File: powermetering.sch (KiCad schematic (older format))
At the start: 143 parts, among them J1 Conn_01x04, J2 Conn_01x02, J3 Conn_01x02, J4 Conn_01x02, J5 Conn_01x02, T1 Transformer_1P_1S, T2 Transformer_1P_1S, T3 Transformer_1P_1S, U2 ADE9000, U7 LTC4055, Y1 Crystal

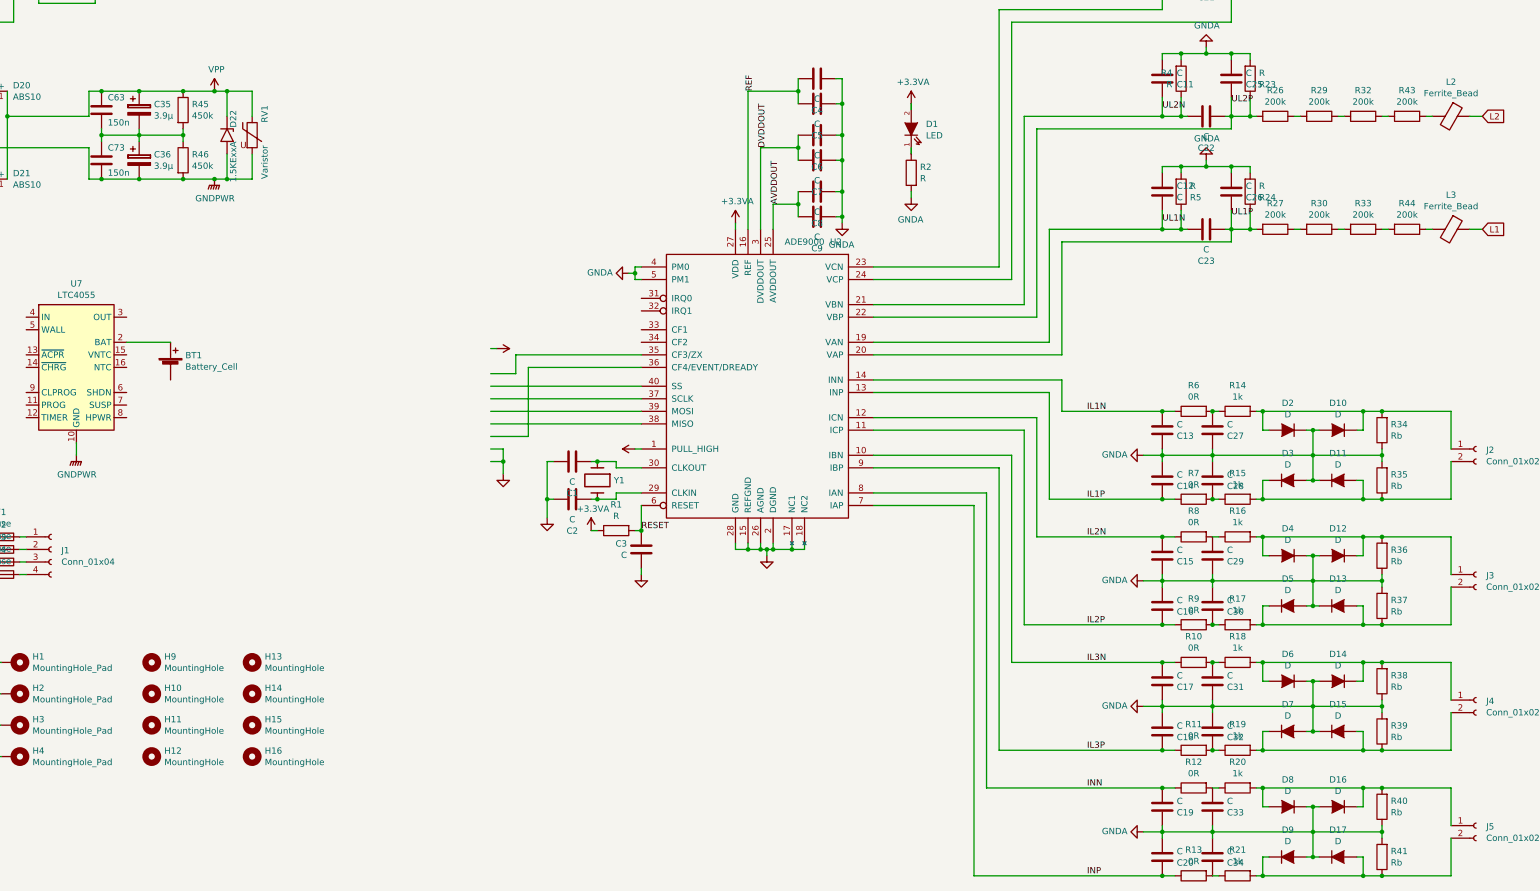
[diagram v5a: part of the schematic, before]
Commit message: Change to bigger housing
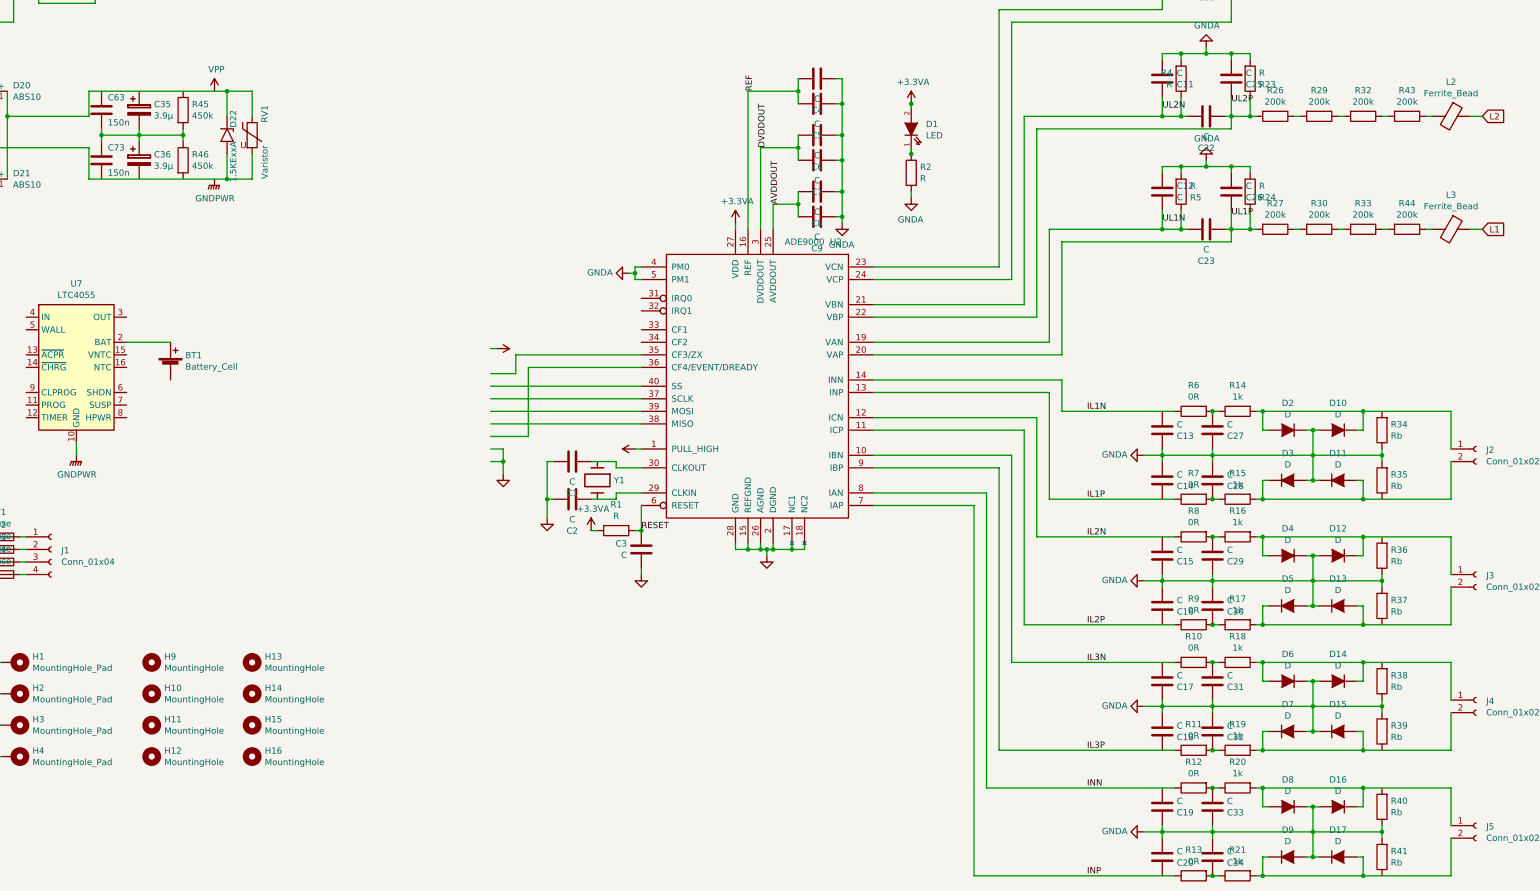
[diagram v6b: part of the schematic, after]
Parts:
- F1, F2, F3, F4: footprint Fuse:Fuse_2920_7451Metric -> Fuse:Fuseholder_Cylinder-6.3x32mm_Schurter_0031-8002_Horizontal_Open
- J1: footprint TerminalBlock_WAGO:TerminalBlock_WAGO-236_2Stift_RM5mm_4pol -> TerminalBlock_Phoenix:TerminalBlock_Phoenix_PT-1,5-4-5.0-H_1x04_P5.00mm_Horizontal
- J2, J3, J4, J5: footprint TerminalBlock_WAGO:TerminalBlock_WAGO-236_2Stift_RM5mm_2pol -> TerminalBlock_Phoenix:TerminalBlock_Phoenix_PT-1,5-2-5.0-H_1x02_P5.00mm_Horizontal
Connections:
- wire segments 444 -> 418
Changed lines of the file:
@@
-EESchema Schematic File Version 4
+EESchema Schematic File Version 5
+LIBS:powermetering-cache
 EELAYER 29 0
 EELAYER END
@@
 F 0 "J1" H 3780 6942 50  0000 L CNN
 F 1 "Conn_01x04" H 3780 6851 50  0000 L CNN
-F 2 "TerminalBlock_WAGO:TerminalBlock_WAGO-236_2Stift_RM5mm_4pol" H 3700 6950 50  0001 C CNN
+F 2 "TerminalBlock_Phoenix:TerminalBlock_Phoenix_PT-1,5-4-5.0-H_1x04_P5.00mm_Horizontal" H 3700 6950 50  0001 C CNN
 F 3 "~" H 3700 6950 50  0001 C CNN
 	1    3700 6950
@@
 F 0 "F1" V 3103 6850 50  0000 C CNN
 F 1 "Fuse" V 3194 6850 50  0000 C CNN
-F 2 "Fuse:Fuse_2920_7451Metric" V 3230 6850 50  0001 C CNN
+F 2 "Fuse:Fuseholder_Cylinder-6.3x32mm_Schurter_0031-8002_Horizontal_Open" V 3230 6850 50  0001 C CNN
 F 3 "" H 3300 6850 50  0001 C CNN
 	1    3300 6850
@@
 F 0 "J2" H 15130 6142 50  0000 L CNN
 F 1 "Conn_01x02" H 15130 6051 50  0000 L CNN
-F 2 "TerminalBlock_WAGO:TerminalBlock_WAGO-236_2Stift_RM5mm_2pol" H 15050 6150 50  0001 C CNN
+F 2 "TerminalBlock_Phoenix:TerminalBlock_Phoenix_PT-1,5-2-5.0-H_1x02_P5.00mm_Horizontal" H 15050 6150 50  0001 C CNN
 F 3 "~" H 15050 6150 50  0001 C CNN
 	1    15050 6150
@@
 $EndComp
 Wire Wire Line
-	14300 6550 14850 6550
-Wire Wire Line
 	14850 6550 14850 6250
-Wire Wire Line
-	14300 5850 14850 5850
 Wire Wire Line
 	14850 5850 14850 6150
@@
 Wire Wire Line
 	13300 6550 13350 6550
-Connection ~ 14300 6550
 Wire Wire Line
 	13300 5850 13350 5850
-Connection ~ 14300 5850
 Wire Wire Line
 	13400 6400 13350 6400
@@
 Connection ~ 14150 6550
 Wire Wire Line
-	14150 6550 14300 6550
-Wire Wire Line
 	13700 6400 13750 6400
 Wire Wire Line
@@
 	14150 6000 14150 5850
 Connection ~ 14150 5850
-Wire Wire Line
-	14150 5850 14300 5850
 Wire Wire Line
 	13400 6000 13350 6000
@@
 F 0 "J3" H 15130 7142 50  0000 L CNN
 F 1 "Conn_01x02" H 15130 7051 50  0000 L CNN
-F 2 "TerminalBlock_WAGO:TerminalBlock_WAGO-236_2Stift_RM5mm_2pol" H 15050 7150 50  0001 C CNN
+F 2 "TerminalBlock_Phoenix:TerminalBlock_Phoenix_PT-1,5-2-5.0-H_1x02_P5.00mm_Horizontal" H 15050 7150 50  0001 C CNN
 F 3 "~" H 15050 7150 50  0001 C CNN
 	1    15050 7150
@@
 $EndComp
 Wire Wire Line
-	14300 7550 14850 7550
-Wire Wire Line
 	14850 7550 14850 7250
-Wire Wire Line
-	14300 6850 14850 6850
 Wire Wire Line
 	14850 6850 14850 7150
@@
 Wire Wire Line
 	13300 7550 13350 7550
-Connection ~ 14300 7550
 Wire Wire Line
 	13300 6850 13350 6850
-Connection ~ 14300 6850
 Wire Wire Line
 	13400 7400 13350 7400
@@
 Connection ~ 14150 7550
 Wire Wire Line
-	14150 7550 14300 7550
-Wire Wire Line
 	13700 7400 13750 7400
 Wire Wire Line
@@
 	14150 7000 14150 6850
 Connection ~ 14150 6850
-Wire Wire Line
-	14150 6850 14300 6850
 Wire Wire Line
 	13400 7000 13350 7000
@@
 F 0 "J4" H 15130 8142 50  0000 L CNN
 F 1 "Conn_01x02" H 15130 8051 50  0000 L CNN
-F 2 "TerminalBlock_WAGO:TerminalBlock_WAGO-236_2Stift_RM5mm_2pol" H 15050 8150 50  0001 C CNN
+F 2 "TerminalBlock_Phoenix:TerminalBlock_Phoenix_PT-1,5-2-5.0-H_1x02_P5.00mm_Horizontal" H 15050 8150 50  0001 C CNN
 F 3 "~" H 15050 8150 50  0001 C CNN
 	1    15050 8150
@@
 $EndComp
 Wire Wire Line
-	14300 8550 14850 8550
-Wire Wire Line
 	14850 8550 14850 8250
-Wire Wire Line
-	14300 7850 14850 7850
 Wire Wire Line
 	14850 7850 14850 8150
@@
 Wire Wire Line
 	13300 8550 13350 8550
-Connection ~ 14300 8550
 Wire Wire Line
 	13300 7850 13350 7850
-Connection ~ 14300 7850
 Wire Wire Line
 	13400 8400 13350 8400
@@
 Connection ~ 14150 8550
 Wire Wire Line
-	14150 8550 14300 8550
-Wire Wire Line
 	13700 8400 13750 8400
 Wire Wire Line
@@
 	14150 8000 14150 7850
 Connection ~ 14150 7850
-Wire Wire Line
-	14150 7850 14300 7850
 Wire Wire Line
 	13400 8000 13350 8000
@@
 F 0 "J5" H 15130 9142 50  0000 L CNN
 F 1 "Conn_01x02" H 15130 9051 50  0000 L CNN
-F 2 "TerminalBlock_WAGO:TerminalBlock_WAGO-236_2Stift_RM5mm_2pol" H 15050 9150 50  0001 C CNN
+F 2 "TerminalBlock_Phoenix:TerminalBlock_Phoenix_PT-1,5-2-5.0-H_1x02_P5.00mm_Horizontal" H 15050 9150 50  0001 C CNN
 F 3 "~" H 15050 9150 50  0001 C CNN
 	1    15050 9150
@@
 $EndComp
 Wire Wire Line
-	14300 9550 14850 9550
-Wire Wire Line
 	14850 9550 14850 9250
-Wire Wire Line
-	14300 8850 14850 8850
 Wire Wire Line
 	14850 8850 14850 9150
@@
 Wire Wire Line
 	13300 9550 13350 9550
-Connection ~ 14300 9550
 Wire Wire Line
 	13300 8850 13350 8850
-Connection ~ 14300 8850
 Wire Wire Line
 	13400 9400 13350 9400
@@
 Connection ~ 14150 9550
 Wire Wire Line
-	14150 9550 14300 9550
-Wire Wire Line
 	13700 9400 13750 9400
 Wire Wire Line
@@
 	14150 9000 14150 8850
 Connection ~ 14150 8850
-Wire Wire Line
-	14150 8850 14300 8850
 Wire Wire Line
 	13400 9000 13350 9000
@@
 F 0 "F2" V 3103 6950 50  0000 C CNN
 F 1 "Fuse" V 3194 6950 50  0000 C CNN
-F 2 "Fuse:Fuse_2920_7451Metric" V 3230 6950 50  0001 C CNN
+F 2 "Fuse:Fuseholder_Cylinder-6.3x32mm_Schurter_0031-8002_Horizontal_Open" V 3230 6950 50  0001 C CNN
 F 3 "" H 3300 6950 50  0001 C CNN
 	1    3300 6950
@@
 F 0 "F3" V 3103 7050 50  0000 C CNN
 F 1 "Fuse" V 3194 7050 50  0000 C CNN
-F 2 "Fuse:Fuse_2920_7451Metric" V 3230 7050 50  0001 C CNN
+F 2 "Fuse:Fuseholder_Cylinder-6.3x32mm_Schurter_0031-8002_Horizontal_Open" V 3230 7050 50  0001 C CNN
 F 3 "" H 3300 7050 50  0001 C CNN
 	1    3300 7050
@@
 F 0 "F4" V 3103 7150 50  0000 C CNN
 F 1 "Fuse" V 3194 7150 50  0000 C CNN
-F 2 "Fuse:Fuse_2920_7451Metric" V 3230 7150 50  0001 C CNN
+F 2 "Fuse:Fuseholder_Cylinder-6.3x32mm_Schurter_0031-8002_Horizontal_Open" V 3230 7150 50  0001 C CNN
 F 3 "" H 3300 7150 50  0001 C CNN
 	1    3300 7150
@@
 Wire Wire Line
 	12950 6200 12950 6250
-Wire Wire Line
-	11750 5850 12550 5850
-Wire Wire Line
-	11550 6850 12550 6850
-Wire Wire Line
-	11450 7550 12550 7550
-Wire Wire Line
-	11350 7850 12550 7850
-Wire Wire Line
-	11250 8550 12550 8550
-Wire Wire Line
-	11150 8850 12550 8850
-Wire Wire Line
-	11050 9550 12550 9550
-Wire Wire Line
-	8000 6550 8050 6550
-Wire Wire Line
-	8000 6250 8050 6250
-Wire Wire Line
-	11650 6550 12550 6550
-Connection ~ 8050 6250
-Wire Wire Line
-	8050 6250 8200 6250
-Connection ~ 8050 6550
-Wire Wire Line
-	8050 6550 8200 6550
 $Comp
 L powermetering:Transformer_1P_1S T1
@@
 Text Label 12550 4350 0    50   ~ 0
 UL1N
-Connection ~ 12550 5850
-Wire Wire Line
-	12550 5850 12650 5850
-Connection ~ 12550 6850
-Wire Wire Line
-	12550 6850 12650 6850
-Connection ~ 12550 7850
-Wire Wire Line
-	12550 7850 12650 7850
-Connection ~ 12550 7550
-Wire Wire Line
-	12550 7550 12650 7550
-Connection ~ 12950 7550
-Connection ~ 12550 6550
-Wire Wire Line
-	12550 6550 12650 6550
-Connection ~ 12950 6550
-Connection ~ 12950 5850
-Connection ~ 12950 7850
-Connection ~ 12550 8550
-Wire Wire Line
-	12550 8550 12650 8550
-Connection ~ 12950 8550
 Text Label 11950 5850 0    50   ~ 0
 IL1N
@@
 Text Label 11950 8850 0    50   ~ 0
 INN
-Connection ~ 12550 8850
-Wire Wire Line
-	12550 8850 12650 8850
-Connection ~ 12550 9550
-Wire Wire Line
-	12550 9550 12650 9550
-Connection ~ 8400 6800
 Text Label 9500 4200 1    50   ~ 0
 AVDDOUT
@@
 Wire Wire Line
 	5050 1500 5050 1250
-Wire Wire Line
-	4000 3300 4100 3300
 $Comp
 L stmbl:R R46
@@
 $EndComp
 Wire Wire Line
-	4400 3300 4750 3300
-Connection ~ 4400 3300
-Wire Wire Line
 	4400 3600 4400 3650
 Wire Wire Line
@@
 Wire Wire Line
 	4750 3650 4750 3700
-Wire Wire Line
-	4000 4000 4100 4000
 $Comp
 L stmbl:CP C36
@@
 	1    0    0    -1
 $EndComp
-Connection ~ 4400 4000
-Wire Wire Line
-	4400 4000 4750 4000
 $Comp
 L Diode:1.5KExxA D22
@@
 $EndComp
 Wire Wire Line
-	4750 3300 5000 3300
-Wire Wire Line
 	5100 3300 5100 3500
-Connection ~ 4750 3300
-Wire Wire Line
-	4750 4000 5000 4000
 Wire Wire Line
 	5100 4000 5100 3800
-Connection ~ 4750 4000
 $Comp
 L Device:Varistor RV1
@@
 	1    0    0    -1
 $EndComp
-Connection ~ 5000 3300
-Wire Wire Line
-	5000 3300 5100 3300
 $Comp
 L stmbl:GNDPWR #PWR0173
@@
 	1    0    0    -1
 $EndComp
-Connection ~ 5000 4000
-Wire Wire Line
-	5000 4000 5100 4000
 $Comp
 L stmbl:C C63
@@
 	1    0    0    -1
 $EndComp
-Connection ~ 4100 3300
-Wire Wire Line
-	4100 3300 4400 3300
 $Comp
 L stmbl:C C73
@@
 	1    0    0    -1
 $EndComp
-Connection ~ 4100 4000
-Wire Wire Line
-	4100 4000 4400 4000
 Wire Wire Line
 	4100 3600 4100 3650
@@
 Wire Wire Line
 	3900 6100 3900 6200
+Wire Wire Line
+	14150 6550 14850 6550
+Wire Wire Line
+	14150 5850 14850 5850
+Wire Wire Line
+	14150 7550 14850 7550
+Wire Wire Line
+	14150 6850 14850 6850
+Wire Wire Line
+	14150 8550 14850 8550
+Wire Wire Line
+	14150 7850 14850 7850
+Wire Wire Line
+	14150 9550 14850 9550
+Wire Wire Line
+	14150 8850 14850 8850
+Wire Wire Line
+	11750 5850 12650 5850
+Wire Wire Line
+	11550 6850 12650 6850
+Wire Wire Line
+	11450 7550 12650 7550
+Wire Wire Line
+	11350 7850 12650 7850
+Wire Wire Line
+	11250 8550 12650 8550
+Wire Wire Line
+	11150 8850 12650 8850
+Wire Wire Line
+	11050 9550 12650 9550
+Wire Wire Line
+	8000 6550 8200 6550
+Wire Wire Line
+	8000 6250 8200 6250
+Wire Wire Line
+	11650 6550 12650 6550
+Wire Wire Line
+	4000 3300 5100 3300
+Wire Wire Line
+	4000 4000 5100 4000
+Connection ~ 12950 5850
+Connection ~ 12950 6550
+Connection ~ 12950 6850
+Connection ~ 12950 7550
+Connection ~ 12950 7850
+Connection ~ 12950 8550
+Connection ~ 12950 8850
+Connection ~ 12950 9550
+Connection ~ 8400 6800
+Connection ~ 10550 3800
+Connection ~ 10550 3400
 $EndSCHEMATC
